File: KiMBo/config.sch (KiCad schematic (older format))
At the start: 18 parts, among them SW3 uSD_Boot

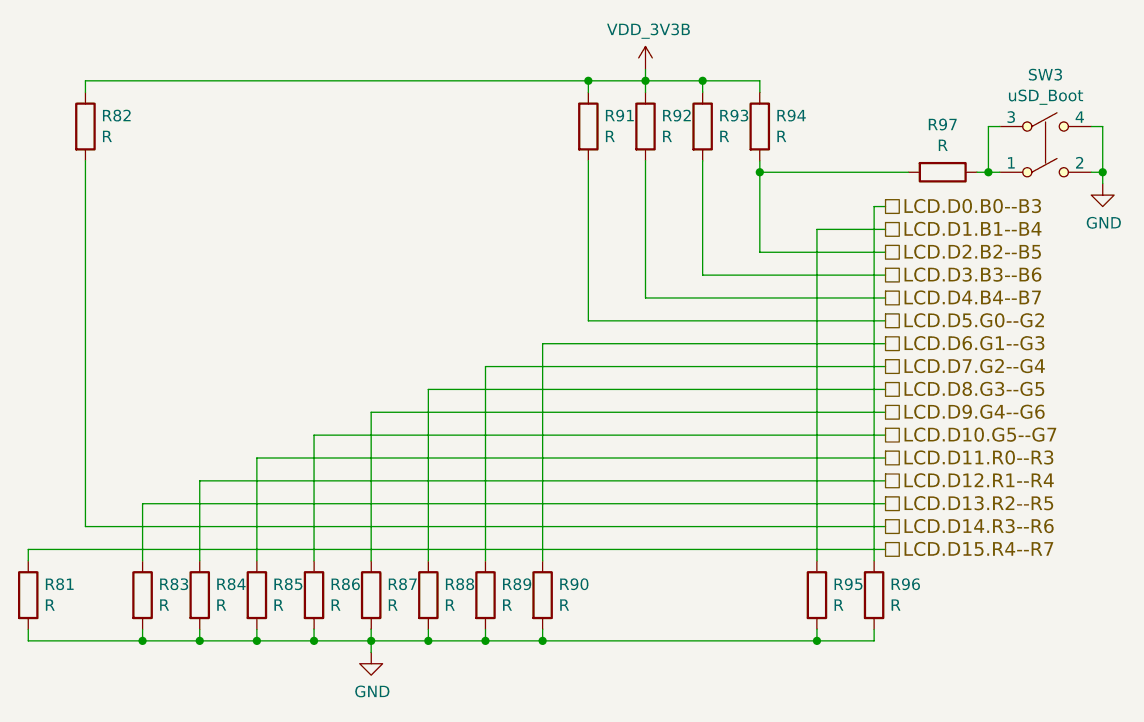
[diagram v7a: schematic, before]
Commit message: Clean up various parts of the schematic, high level sheet has annoated modules
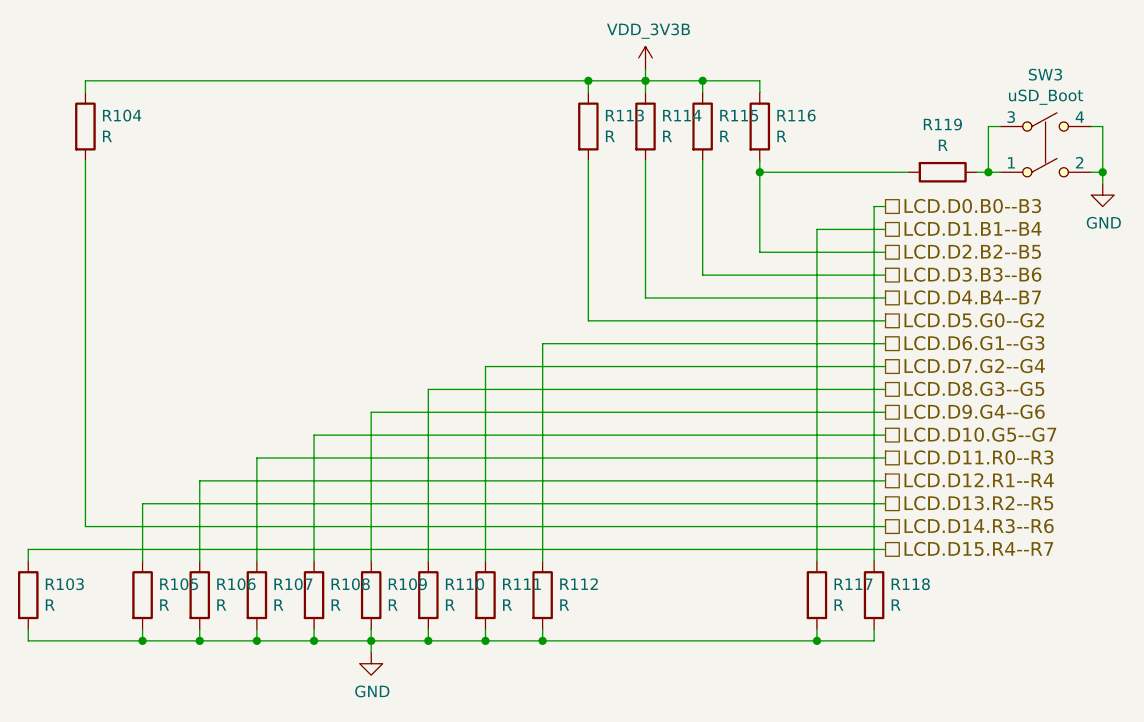
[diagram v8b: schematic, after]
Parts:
- renumbered R81 to R103, R82 to R104, R83 to R105, R84 to R106, R85 to R107, R86 to R108, R87 to R109, R88 to R110, R89 to R111, R90 to R112, R91 to R113, R92 to R114, R93 to R115, R94 to R116, R95 to R117, R96 to R118, R97 to R119
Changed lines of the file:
@@
 $Descr A4 11693 8268
 encoding utf-8
-Sheet 12 26
+Sheet 11 26
 Title ""
 Date ""
@@
 $EndDescr
 $Comp
-L R R?
+L R R107
 U 1 1 58A2324A
 P 4200 3600
-AR Path="/589C2BEE/58A2324A" Ref="R?"  Part="1"
-AR Path="/58958D2E/5AD44766/58A2324A" Ref="R85"  Part="1"
-F 0 "R85" H 4270 3646 50  0000 L CNN
+F 0 "R107" H 4270 3646 50  0000 L CNN
 F 1 "R" H 4270 3555 50  0000 L CNN
 F 2 "" V 4130 3600 50  0000 C CNN
@@
 $EndComp
 $Comp
-L R R?
+L R R108
 U 1 1 58A2326A
 P 4450 3600
-AR Path="/589C2BEE/58A2326A" Ref="R?"  Part="1"
-AR Path="/58958D2E/5AD44766/58A2326A" Ref="R86"  Part="1"
-F 0 "R86" H 4520 3646 50  0000 L CNN
+F 0 "R108" H 4520 3646 50  0000 L CNN
 F 1 "R" H 4520 3555 50  0000 L CNN
 F 2 "" V 4380 3600 50  0000 C CNN
@@
 $EndComp
 $Comp
-L R R?
+L R R109
 U 1 1 58A2328E
 P 4700 3600
-AR Path="/589C2BEE/58A2328E" Ref="R?"  Part="1"
-AR Path="/58958D2E/5AD44766/58A2328E" Ref="R87"  Part="1"
-F 0 "R87" H 4770 3646 50  0000 L CNN
+F 0 "R109" H 4770 3646 50  0000 L CNN
 F 1 "R" H 4770 3555 50  0000 L CNN
 F 2 "" V 4630 3600 50  0000 C CNN
@@
 $EndComp
 $Comp
-L R R?
+L R R110
 U 1 1 58A232B1
 P 4950 3600
-AR Path="/589C2BEE/58A232B1" Ref="R?"  Part="1"
-AR Path="/58958D2E/5AD44766/58A232B1" Ref="R88"  Part="1"
-F 0 "R88" H 5020 3646 50  0000 L CNN
+F 0 "R110" H 5020 3646 50  0000 L CNN
 F 1 "R" H 5020 3555 50  0000 L CNN
 F 2 "" V 4880 3600 50  0000 C CNN
@@
 $EndComp
 $Comp
-L R R?
+L R R111
 U 1 1 58A232DB
 P 5200 3600
-AR Path="/589C2BEE/58A232DB" Ref="R?"  Part="1"
-AR Path="/58958D2E/5AD44766/58A232DB" Ref="R89"  Part="1"
-F 0 "R89" H 5270 3646 50  0000 L CNN
+F 0 "R111" H 5270 3646 50  0000 L CNN
 F 1 "R" H 5270 3555 50  0000 L CNN
 F 2 "" V 5130 3600 50  0000 C CNN
@@
 $EndComp
 $Comp
-L R R?
+L R R112
 U 1 1 58A23304
 P 5450 3600
-AR Path="/589C2BEE/58A23304" Ref="R?"  Part="1"
-AR Path="/58958D2E/5AD44766/58A23304" Ref="R90"  Part="1"
-F 0 "R90" H 5520 3646 50  0000 L CNN
+F 0 "R112" H 5520 3646 50  0000 L CNN
 F 1 "R" H 5520 3555 50  0000 L CNN
 F 2 "" V 5380 3600 50  0000 C CNN
@@
 $EndComp
 $Comp
-L R R?
+L R R117
 U 1 1 58A23332
 P 6650 3600
-AR Path="/589C2BEE/58A23332" Ref="R?"  Part="1"
-AR Path="/58958D2E/5AD44766/58A23332" Ref="R95"  Part="1"
-F 0 "R95" H 6720 3646 50  0000 L CNN
+F 0 "R117" H 6720 3646 50  0000 L CNN
 F 1 "R" H 6720 3555 50  0000 L CNN
 F 2 "" V 6580 3600 50  0000 C CNN
@@
 $EndComp
 $Comp
-L R R?
+L R R118
 U 1 1 58A23361
 P 6900 3600
-AR Path="/589C2BEE/58A23361" Ref="R?"  Part="1"
-AR Path="/58958D2E/5AD44766/58A23361" Ref="R96"  Part="1"
-F 0 "R96" H 6970 3646 50  0000 L CNN
+F 0 "R118" H 6970 3646 50  0000 L CNN
 F 1 "R" H 6970 3555 50  0000 L CNN
 F 2 "" V 6830 3600 50  0000 C CNN
@@
 LCD.D11.R0--R3
 $Comp
-L R R?
+L R R106
 U 1 1 58A25F63
 P 3950 3600
-AR Path="/589C2BEE/58A25F63" Ref="R?"  Part="1"
-AR Path="/58958D2E/5AD44766/58A25F63" Ref="R84"  Part="1"
-F 0 "R84" H 4020 3646 50  0000 L CNN
+F 0 "R106" H 4020 3646 50  0000 L CNN
 F 1 "R" H 4020 3555 50  0000 L CNN
 F 2 "" V 3880 3600 50  0000 C CNN
@@
 $EndComp
 $Comp
-L R R?
+L R R105
 U 1 1 58A25F94
 P 3700 3600
-AR Path="/589C2BEE/58A25F94" Ref="R?"  Part="1"
-AR Path="/58958D2E/5AD44766/58A25F94" Ref="R83"  Part="1"
-F 0 "R83" H 3770 3646 50  0000 L CNN
+F 0 "R105" H 3770 3646 50  0000 L CNN
 F 1 "R" H 3770 3555 50  0000 L CNN
 F 2 "" V 3630 3600 50  0000 C CNN
@@
 $EndComp
 $Comp
-L R R?
+L R R103
 U 1 1 58A260DB
 P 3200 3600
-AR Path="/589C2BEE/58A260DB" Ref="R?"  Part="1"
-AR Path="/58958D2E/5AD44766/58A260DB" Ref="R81"  Part="1"
-F 0 "R81" H 3270 3646 50  0000 L CNN
+F 0 "R103" H 3270 3646 50  0000 L CNN
 F 1 "R" H 3270 3555 50  0000 L CNN
 F 2 "" V 3130 3600 50  0000 C CNN
@@
 $EndComp
 $Comp
-L GND #PWR?
+L GND #PWR0172
 U 1 1 58A262E3
 P 4700 3850
-AR Path="/589C2BEE/58A262E3" Ref="#PWR?"  Part="1"
-AR Path="/58958D2E/5AD44766/58A262E3" Ref="#PWR0172"  Part="1"
 F 0 "#PWR0172" H 4700 3600 50  0001 C CNN
 F 1 "GND" H 4705 3677 50  0000 C CNN
@@
 $EndComp
 $Comp
-L R R?
+L R R116
 U 1 1 58A26A66
 P 6400 1550
-AR Path="/589C2BEE/58A26A66" Ref="R?"  Part="1"
-AR Path="/58958D2E/5AD44766/58A26A66" Ref="R94"  Part="1"
-F 0 "R94" H 6470 1596 50  0000 L CNN
+F 0 "R116" H 6470 1596 50  0000 L CNN
 F 1 "R" H 6470 1505 50  0000 L CNN
 F 2 "" V 6330 1550 50  0000 C CNN
@@
 $EndComp
 $Comp
-L R R?
+L R R115
 U 1 1 58A26AC4
 P 6150 1550
-AR Path="/589C2BEE/58A26AC4" Ref="R?"  Part="1"
-AR Path="/58958D2E/5AD44766/58A26AC4" Ref="R93"  Part="1"
-F 0 "R93" H 6220 1596 50  0000 L CNN
+F 0 "R115" H 6220 1596 50  0000 L CNN
 F 1 "R" H 6220 1505 50  0000 L CNN
 F 2 "" V 6080 1550 50  0000 C CNN
@@
 $EndComp
 $Comp
-L R R?
+L R R114
 U 1 1 58A26B05
 P 5900 1550
-AR Path="/589C2BEE/58A26B05" Ref="R?"  Part="1"
-AR Path="/58958D2E/5AD44766/58A26B05" Ref="R92"  Part="1"
-F 0 "R92" H 5970 1596 50  0000 L CNN
+F 0 "R114" H 5970 1596 50  0000 L CNN
 F 1 "R" H 5970 1505 50  0000 L CNN
 F 2 "" V 5830 1550 50  0000 C CNN
@@
 $EndComp
 $Comp
-L R R?
+L R R113
 U 1 1 58A26B4F
 P 5650 1550
-AR Path="/589C2BEE/58A26B4F" Ref="R?"  Part="1"
-AR Path="/58958D2E/5AD44766/58A26B4F" Ref="R91"  Part="1"
-F 0 "R91" H 5720 1596 50  0000 L CNN
+F 0 "R113" H 5720 1596 50  0000 L CNN
 F 1 "R" H 5720 1505 50  0000 L CNN
 F 2 "" V 5580 1550 50  0000 C CNN
@@
 $EndComp
 $Comp
-L R R?
+L R R104
 U 1 1 58A26BA2
 P 3450 1550
-AR Path="/589C2BEE/58A26BA2" Ref="R?"  Part="1"
-AR Path="/58958D2E/5AD44766/58A26BA2" Ref="R82"  Part="1"
-F 0 "R82" H 3520 1596 50  0000 L CNN
+F 0 "R104" H 3520 1596 50  0000 L CNN
 F 1 "R" H 3520 1505 50  0000 L CNN
 F 2 "" V 3380 1550 50  0000 C CNN
@@
 Connection ~ 5650 1350
 $Comp
-L R R?
+L R R119
 U 1 1 58A2A28E
 P 7200 1750
-AR Path="/589C2BEE/58A2A28E" Ref="R?"  Part="1"
-AR Path="/58958D2E/5AD44766/58A2A28E" Ref="R97"  Part="1"
-F 0 "R97" V 6993 1750 50  0000 C CNN
+F 0 "R119" V 6993 1750 50  0000 C CNN
 F 1 "R" V 7084 1750 50  0000 C CNN
 F 2 "" V 7130 1750 50  0000 C CNN
@@
 Connection ~ 6400 1750
 $Comp
-L SW_DPST_Small SW?
+L SW_DPST_Small SW3
 U 1 1 58A2A610
 P 7650 1650
-AR Path="/589C2BEE/58A2A610" Ref="SW?"  Part="1"
-AR Path="/58958D2E/5AD44766/58A2A610" Ref="SW3"  Part="1"
 F 0 "SW3" H 7650 1975 50  0000 C CNN
 F 1 "uSD_Boot" H 7650 1884 50  0000 C CNN
@@
 Connection ~ 7900 1750
 $Comp
-L GND #PWR?
+L GND #PWR0173
 U 1 1 58A2A814
 P 7900 1800
-AR Path="/589C2BEE/58A2A814" Ref="#PWR?"  Part="1"
-AR Path="/58958D2E/5AD44766/58A2A814" Ref="#PWR0173"  Part="1"
 F 0 "#PWR0173" H 7900 1550 50  0001 C CNN
 F 1 "GND" H 7905 1627 50  0000 C CNN
@@
 $EndComp
 $Comp
-L VDD_3V3B #PWR?
+L VDD_3V3B #PWR0174
 U 1 1 5A05FAAA
 P 5900 1300
-AR Path="/589C2BEE/5A05FAAA" Ref="#PWR?"  Part="1"
-AR Path="/58958D2E/5AD44766/5A05FAAA" Ref="#PWR0174"  Part="1"
 F 0 "#PWR0174" H 5900 1150 50  0001 C CNN
 F 1 "VDD_3V3B" H 5915 1473 50  0000 C CNN
